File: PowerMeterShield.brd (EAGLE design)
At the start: 71.1 x 53.3 mm, 35 parts, among them U1 INA170EA/2K5, U2 THS4521, U3 INA138, U4 ADUM1250ARZ, U5 MCP3426A0-E/SN, U6 ISL21080

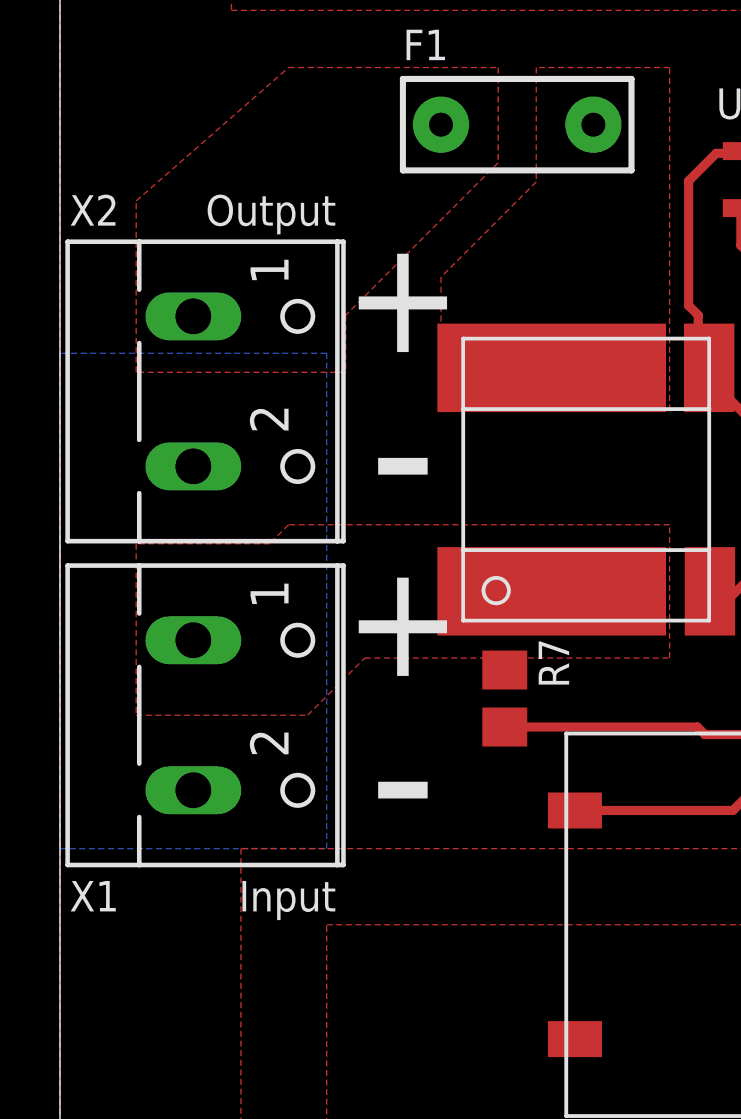
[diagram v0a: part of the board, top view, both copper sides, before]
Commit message: Added prices + order codes
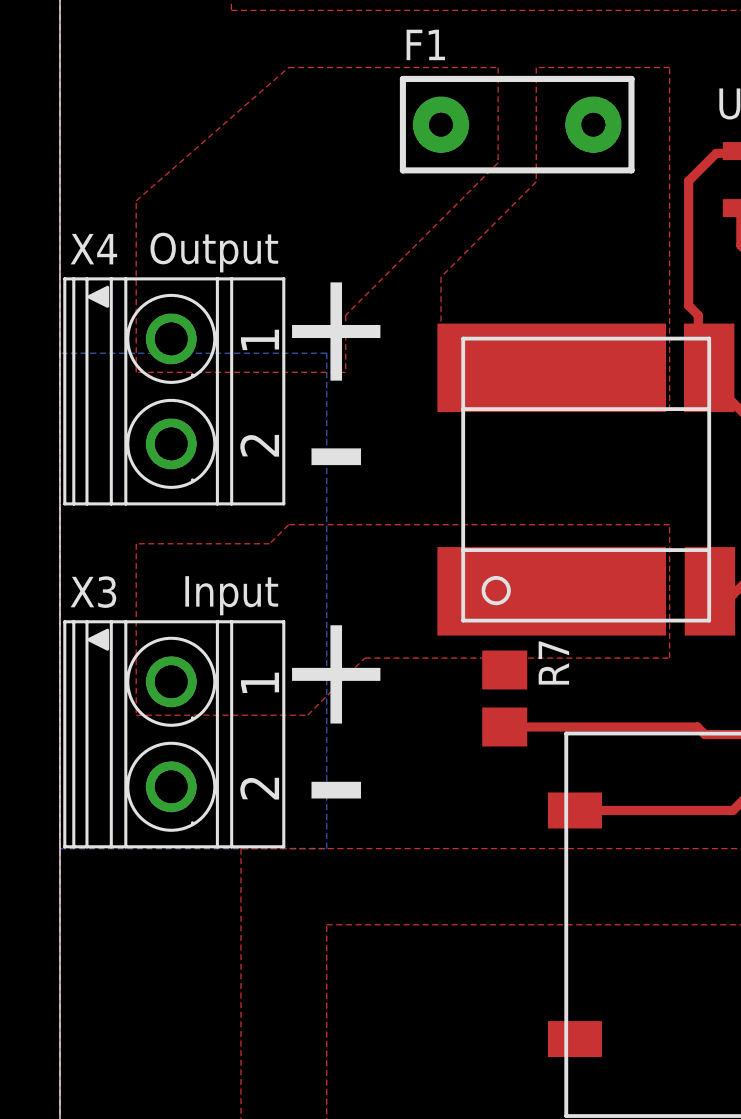
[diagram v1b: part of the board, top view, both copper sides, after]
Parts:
- removed X1, X2: (no value), con-wago-500:W237-102
- added X3, X4: 1751248, con-phoenix-350:1751248
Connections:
- net GNDI: now also X3.2, X4.2; no longer X1.2, X2.2
- net VIN_MEAS: now also X4.1; no longer X2.1
- net V_MEAS: now also X3.1; no longer X1.1

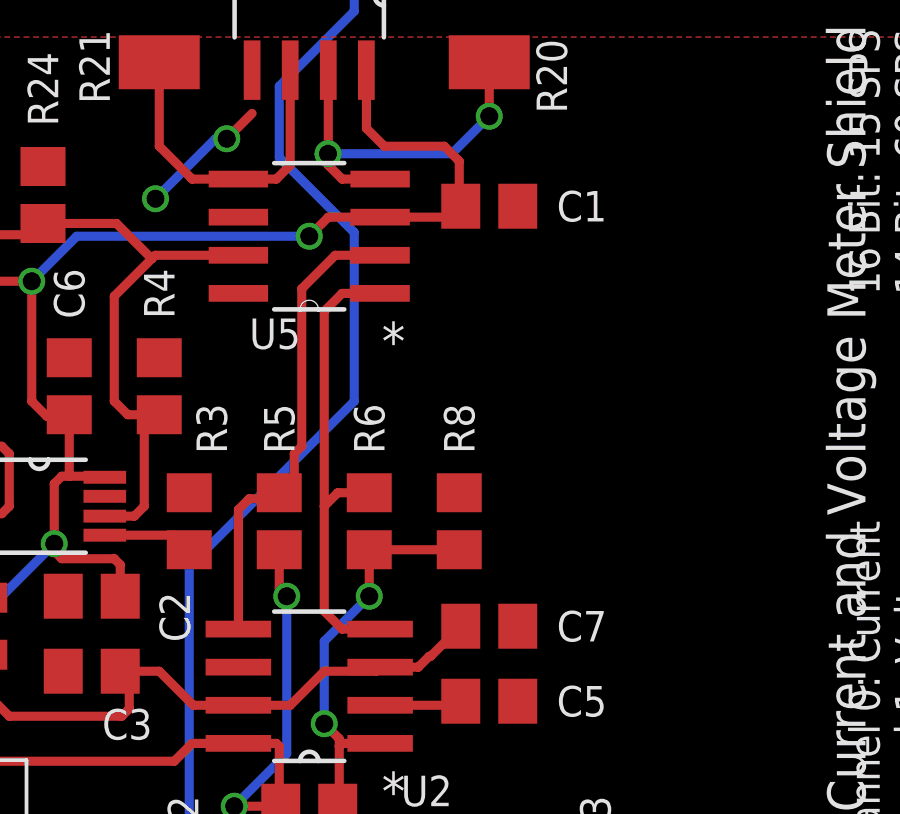
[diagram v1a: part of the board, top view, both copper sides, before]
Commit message: Added experimental serial line resistors and capacitors
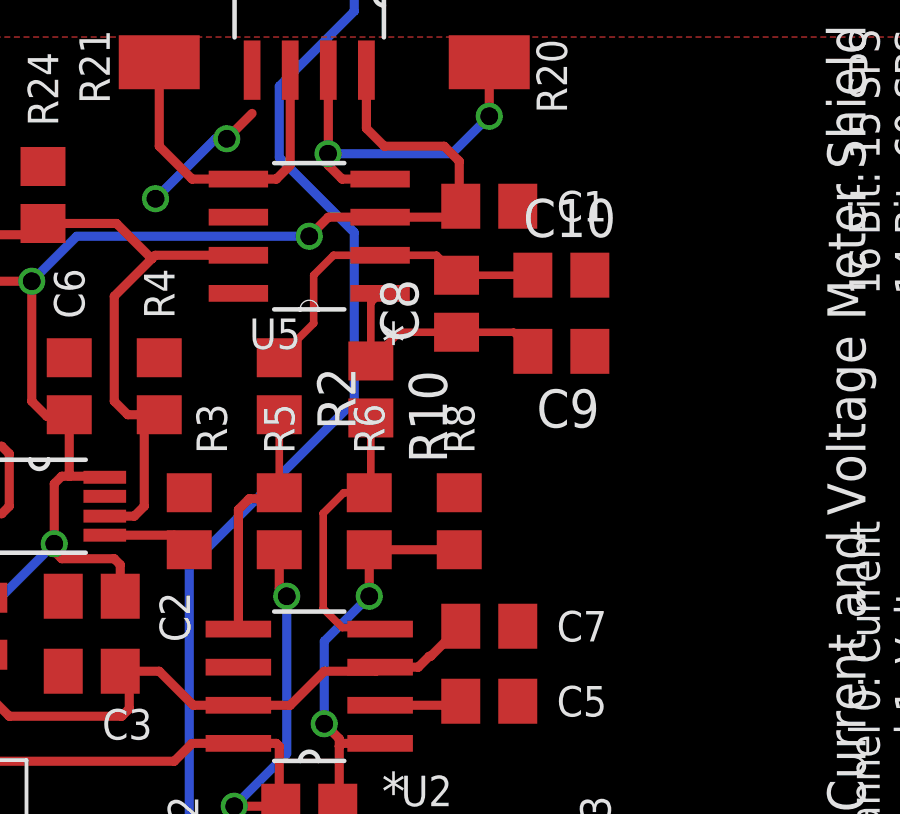
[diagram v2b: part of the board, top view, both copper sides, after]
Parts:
- added C10, C8, C9: 10n, rcl:C0805
- added R10, R2: 33, rcl:R0805
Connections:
- new net ADC1+_OLD: R10.2, R6.2, U2.4
- new net ADC1-_OLD: R2.2, R5.2, U2.5
- net ADC1+: now also C8.1, C9.2, R10.1; no longer R6.2, U2.4
- net ADC1-: now also C10.1, C8.2, R2.1; no longer R5.2, U2.5
- net GNDI: now also C10.2, C9.1
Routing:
- net ADC1+_OLD: track 0.00 -> 9.69 mm
- net ADC1-_OLD: track 0.00 -> 8.18 mm
- net ADC1+: track 15.9 -> 8.44 mm
- net ADC1-: track 15.8 -> 11.1 mm
